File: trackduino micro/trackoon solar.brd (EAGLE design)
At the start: 57.2 x 19.1 mm, 53 parts, among them IC1 MCP73871, IC2 74AHC1G125DBV, SW1 SPST_TACT-KMR2, U1 ATMEGA168MLF, Y1 16MHZ

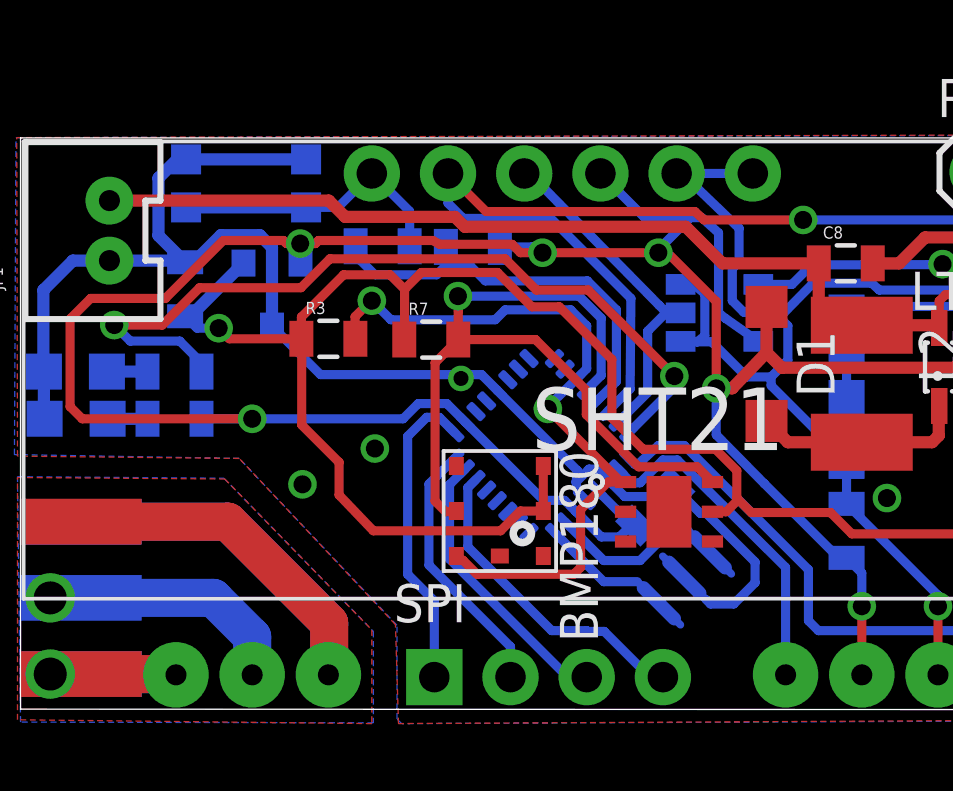
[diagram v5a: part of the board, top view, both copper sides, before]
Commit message: added i2c breakout and fixed ftdi
added breakouts on all versions for i2c next to the spi header, replaced
IO breakout headers from .1" to 2mm to accomodate i2c.
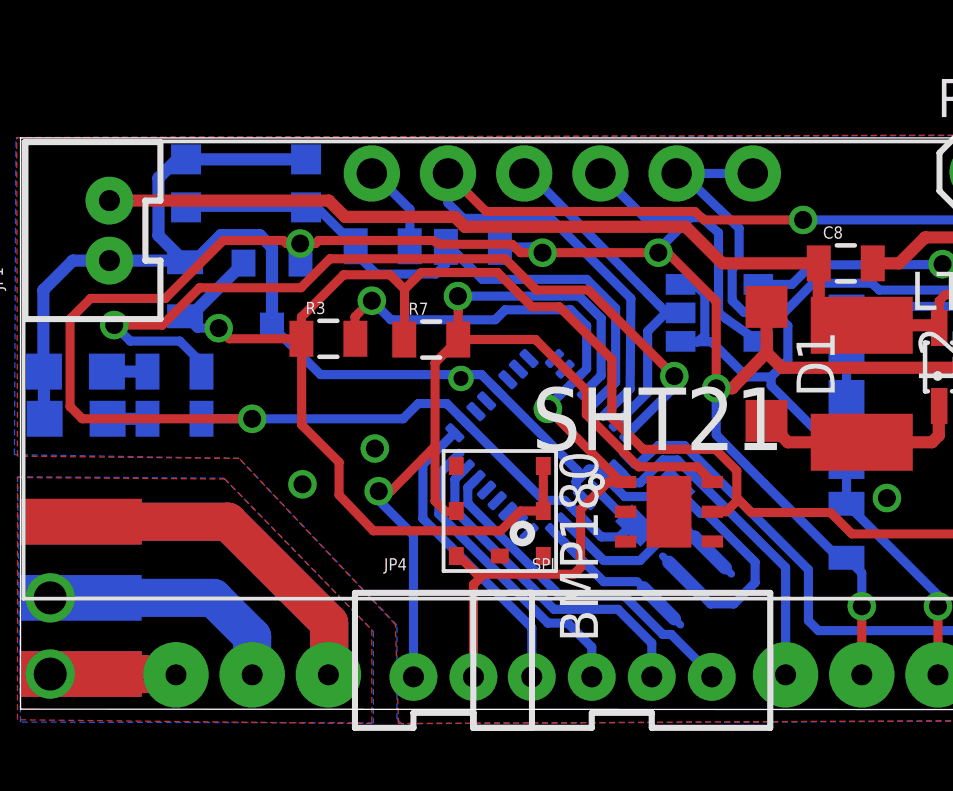
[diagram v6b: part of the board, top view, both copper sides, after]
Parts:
- added JP4: M02JST-PTH-VERT, SparkFun-Connectors:JST-2-PTH-VERT
- SPI: device SparkFun-Connectors:1X04_NO_SILK -> SparkFun-Connectors:JST-4-PTH-VERT
- moved SPI 6.27 mm to (28.9, 13.5)
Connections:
- removed net N$7: C5.2, R5.1, U1.29
- new net N$19: C5.2, R5.1, SW1.1, SW1.3, U1.29
- net DTR: no longer SW1.1, SW1.3
- net SCL: now also JP4.1
- net SDA: now also JP4.2
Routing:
- net N$19: track 0.00 -> 20.3 mm
- net N$7: track 13.9 -> 0.00 mm
- net SCL: track 26.6 -> 35.8 mm, vias 1 -> 2
- net DTR: track 9.61 -> 3.00 mm
- net SDA: track 24.5 -> 28.1 mm
- net MOSI: track 9.43 -> 11.0 mm
- net MISO: track 8.78 -> 10.0 mm
- net SS: track 10.7 -> 11.5 mm

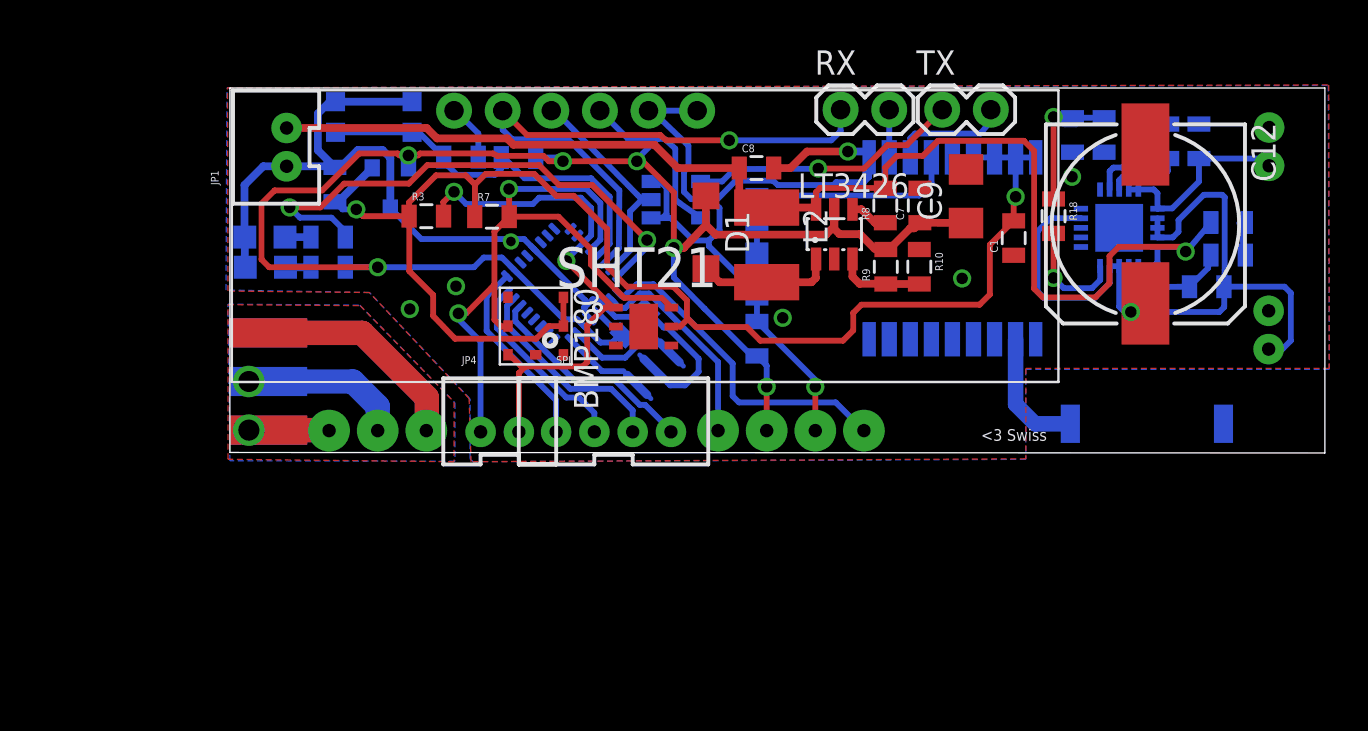
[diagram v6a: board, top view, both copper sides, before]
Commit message: Moved all boards to origin
Moved all the boards such that the lower left most corner is at the
origin.
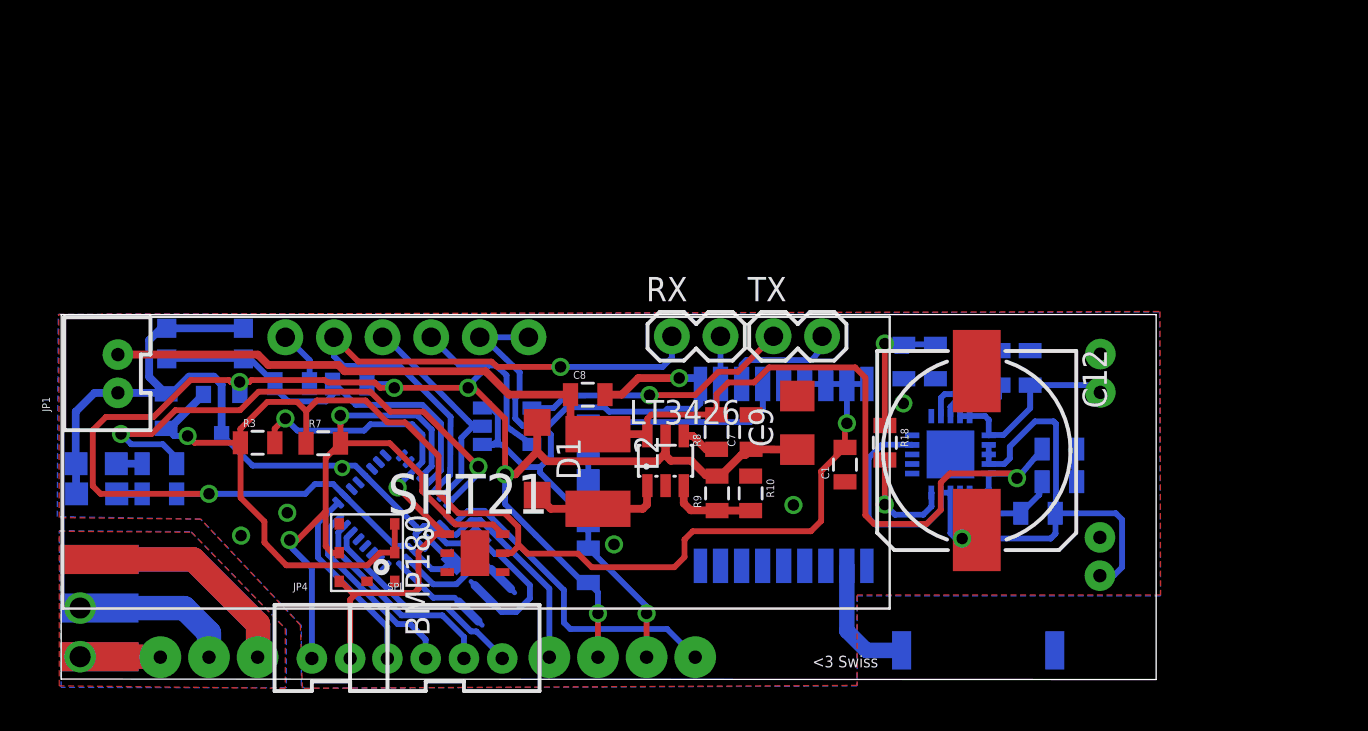
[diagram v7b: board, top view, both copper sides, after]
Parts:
- moved BMP180 14.8 mm to (16.0, 6.60)
- moved C8 14.8 mm to (27.5, 14.9)
- moved IC2 14.8 mm to (23.3, 13.2)
- moved L2 14.8 mm to (28.0, 10.8)
- moved LT3426 14.8 mm to (31.6, 11.4)
- moved C1 14.8 mm to (40.9, 11.2)
- moved C10 14.8 mm to (52.1, 12.0)
- moved C11 14.8 mm to (50.6, 16.3)
- moved C12 14.8 mm to (47.8, 11.9)
- moved C2 14.8 mm to (5.49, 14.0)
- moved C3 14.8 mm to (21.2, 6.76)
- moved C4 14.8 mm to (27.5, 5.94)
- moved C5 14.8 mm to (12.1, 15.4)
- moved C7 14.8 mm to (36.0, 12.9)
- moved C9 14.8 mm to (38.5, 13.4)
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
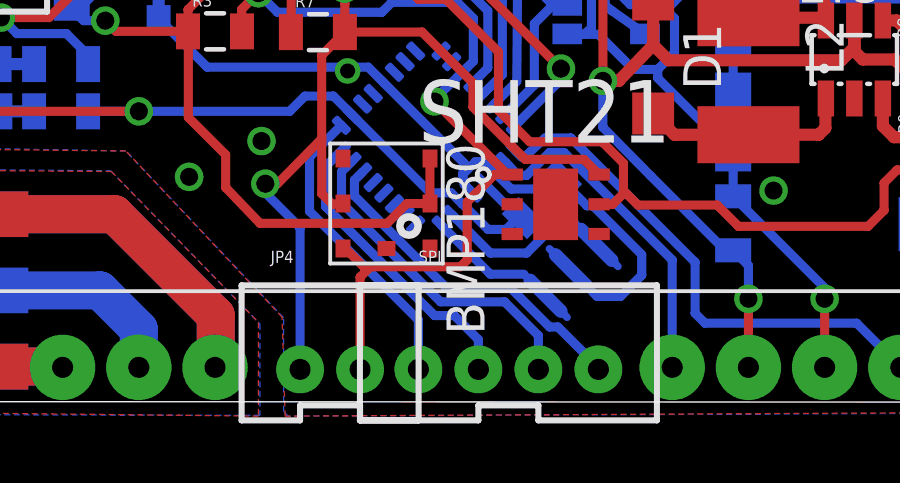
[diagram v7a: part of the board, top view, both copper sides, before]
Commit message: lined up 12c / spi headers
lined up api and i2c headers between the chip, u.fl, and solar versions
of the board.
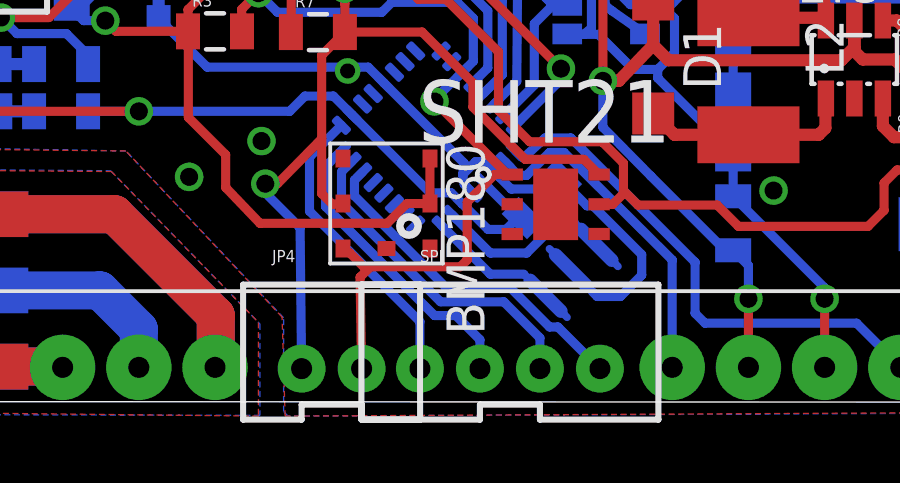
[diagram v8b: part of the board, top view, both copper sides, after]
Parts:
- moved JP4 0.06 mm to (14.1, 1.65)
- moved SPI 0.06 mm to (20.1, 1.65)
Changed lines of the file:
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@@
 <element name="C5" library="SparkFun-Capacitors" package="0805" value=".1uf" x="12.071159375" y="15.427575" rot="MR0"/>
 <element name="TX" library="SparkFun-Connectors" package="1X02" value="TX" x="37.211" y="17.907"/>
-<element name="SPI" library="SparkFun-Connectors" package="JST-4-PTH-VERT" value="" x="20.0406" y="1.6256"/>
+<element name="SPI" library="SparkFun-Connectors" package="JST-4-PTH-VERT" value="" x="20.0914" y="1.651"/>
 <element name="FRAME1" library="SparkFun-Aesthetics" package="CREATIVE_COMMONS" value="FRAME-LETTER" x="14.3764" y="-8.1534"/>
 <element name="PTT" library="adafruit" package="CHIP-LED0805" value="" x="1.8288" y="11.2522" rot="MR270"/>
@@
 <element name="C12" library="adafruit" package="153CLV-1012" value="" x="47.8282" y="11.938" rot="R270"/>
 <element name="U$3" library="SparkFun-RF" package="ANTENNA-CHIP4" value="ANTENNA2SMD3" x="47.9044" y="1.4986" rot="MR180"/>
-<element name="JP4" library="SparkFun-Connectors" package="JST-2-PTH-VERT" value="M02JST-PTH-VERT" x="14.097" y="1.6256"/>
+<element name="JP4" library="SparkFun-Connectors" package="JST-2-PTH-VERT" value="M02JST-PTH-VERT" x="14.1478" y="1.651"/>
 </elements>
 <signals>
@@
 <contactref element="U1" pad="16"/>
 <contactref element="SPI" pad="2"/>
-<wire x1="19.0406" y1="1.0756" x2="19.0406" y2="2.0668" width="0.3048" layer="16"/>
-<wire x1="19.0406" y1="2.0668" x2="18.2372" y2="2.8702" width="0.3048" layer="16"/>
-<wire x1="18.2372" y1="2.8702" x2="17.5768" y2="2.8702" width="0.3048" layer="16"/>
+<wire x1="19.0914" y1="1.101" x2="19.0914" y2="2.0668" width="0.3048" layer="16"/>
+<wire x1="19.0914" y1="2.0668" x2="18.288" y2="2.8702" width="0.3048" layer="16"/>
+<wire x1="18.288" y1="2.8702" x2="17.5768" y2="2.8702" width="0.3048" layer="16"/>
 <wire x1="17.5768" y1="2.8702" x2="13.9446" y2="6.5024" width="0.3048" layer="16"/>
 <wire x1="13.9446" y1="6.5024" x2="13.9446" y2="7.834271875" width="0.3048" layer="16"/>
@@
 <contactref element="U1" pad="15"/>
 <contactref element="SPI" pad="3"/>
-<wire x1="21.0406" y1="1.0756" x2="21.0406" y2="2.2004" width="0.3048" layer="16"/>
-<wire x1="21.0406" y1="2.2004" x2="19.9136" y2="3.3274" width="0.3048" layer="16"/>
-<wire x1="19.9136" y1="3.3274" x2="17.78" y2="3.3274" width="0.3048" layer="16"/>
+<wire x1="21.0914" y1="1.101" x2="21.0914" y2="2.1242" width="0.3048" layer="16"/>
+<wire x1="21.0914" y1="2.1242" x2="19.8882" y2="3.3274" width="0.3048" layer="16"/>
+<wire x1="19.8882" y1="3.3274" x2="17.78" y2="3.3274" width="0.3048" layer="16"/>
 <wire x1="17.78" y1="3.3274" x2="14.478" y2="6.6294" width="0.3048" layer="16"/>
 <wire x1="14.478" y1="6.6294" x2="14.478" y2="7.660565625" width="0.3048" layer="16"/>
@@
 <contactref element="U1" pad="17"/>
 <contactref element="SPI" pad="1"/>
-<wire x1="17.0406" y1="1.0756" x2="17.0406" y2="2.7206" width="0.3048" layer="16"/>
-<wire x1="17.0406" y1="2.7206" x2="13.4112" y2="6.35" width="0.3048" layer="16"/>
+<wire x1="17.0914" y1="1.101" x2="17.0914" y2="2.6698" width="0.3048" layer="16"/>
+<wire x1="17.0914" y1="2.6698" x2="13.4112" y2="6.35" width="0.3048" layer="16"/>
 <wire x1="13.4112" y1="6.35" x2="13.4112" y2="8.1494" width="0.3048" layer="16"/>
 <wire x1="13.4112" y1="8.1494" x2="14.4744625" y2="9.2126625" width="0.3048" layer="16"/>
@@
 <contactref element="U1" pad="14"/>
 <contactref element="SPI" pad="4"/>
-<wire x1="23.0406" y1="1.0756" x2="23.0406" y2="1.1402" width="0.3048" layer="16"/>
+<wire x1="23.0914" y1="1.101" x2="23.0406" y2="1.1402" width="0.3048" layer="16"/>
 <wire x1="23.0406" y1="1.1402" x2="21.6916" y2="2.4892" width="0.3048" layer="16"/>
 <wire x1="21.6916" y1="2.4892" x2="21.4122" y2="2.4892" width="0.3048" layer="16"/>
@@
 <wire x1="17.5768" y1="10.07765625" x2="18.504971875" y2="10.980428125" width="0.3048" layer="16"/>
 <contactref element="JP4" pad="2"/>
-<wire x1="15.097" y1="1.0756" x2="15.097" y2="4.1496" width="0.3048" layer="1"/>
+<wire x1="15.1478" y1="1.101" x2="15.097" y2="4.1496" width="0.3048" layer="1"/>
 <wire x1="15.097" y1="4.1496" x2="15.4432" y2="4.4958" width="0.3048" layer="1"/>
 </signal>
@@
 <wire x1="17.1664" y1="12.319" x2="14.5906" y2="12.319" width="0.3048" layer="1"/>
 <contactref element="JP4" pad="1"/>
-<wire x1="13.097" y1="1.0756" x2="13.097" y2="5.8006" width="0.3048" layer="16"/>
+<wire x1="13.1478" y1="1.101" x2="13.097" y2="5.8006" width="0.3048" layer="16"/>
 <wire x1="13.097" y1="5.8006" x2="11.938" y2="6.9596" width="0.3048" layer="16"/>
 <wire x1="11.938" y1="6.9596" x2="11.938" y2="7.2644" width="0.3048" layer="16"/>
